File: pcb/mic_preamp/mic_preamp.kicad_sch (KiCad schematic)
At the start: 17 parts, among them J1 mic_in, J2 power_input, J3 line_out, U1 THAT1512

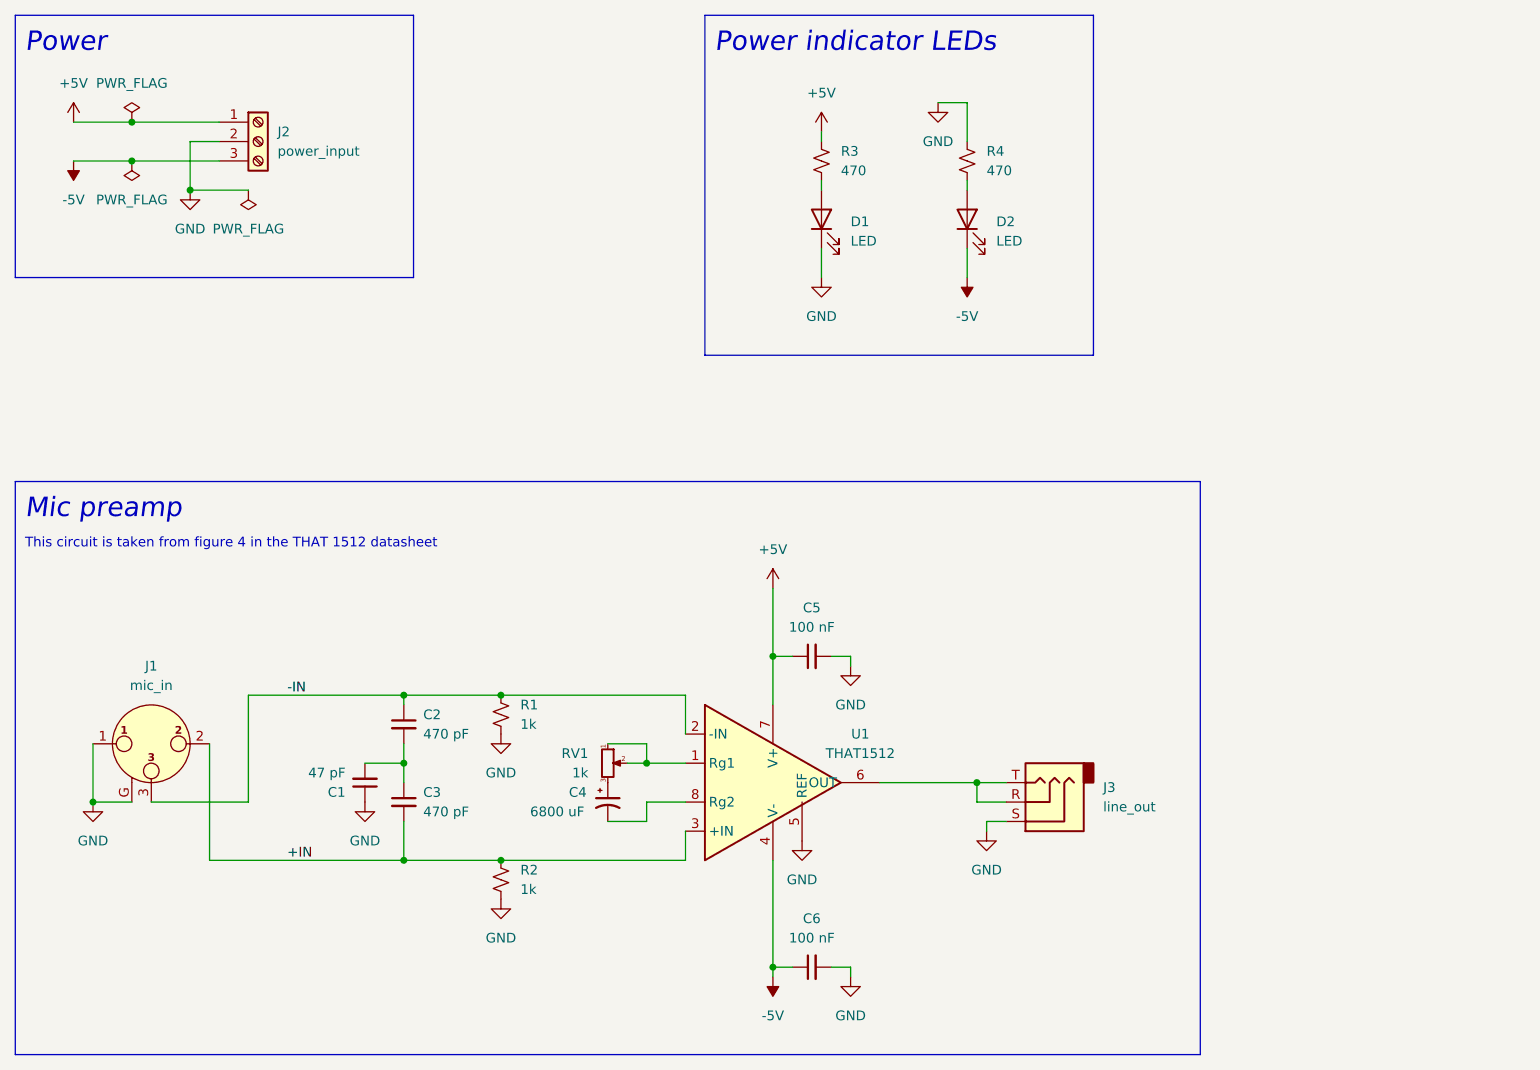
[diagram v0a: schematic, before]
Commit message: mic preamp pcb layout
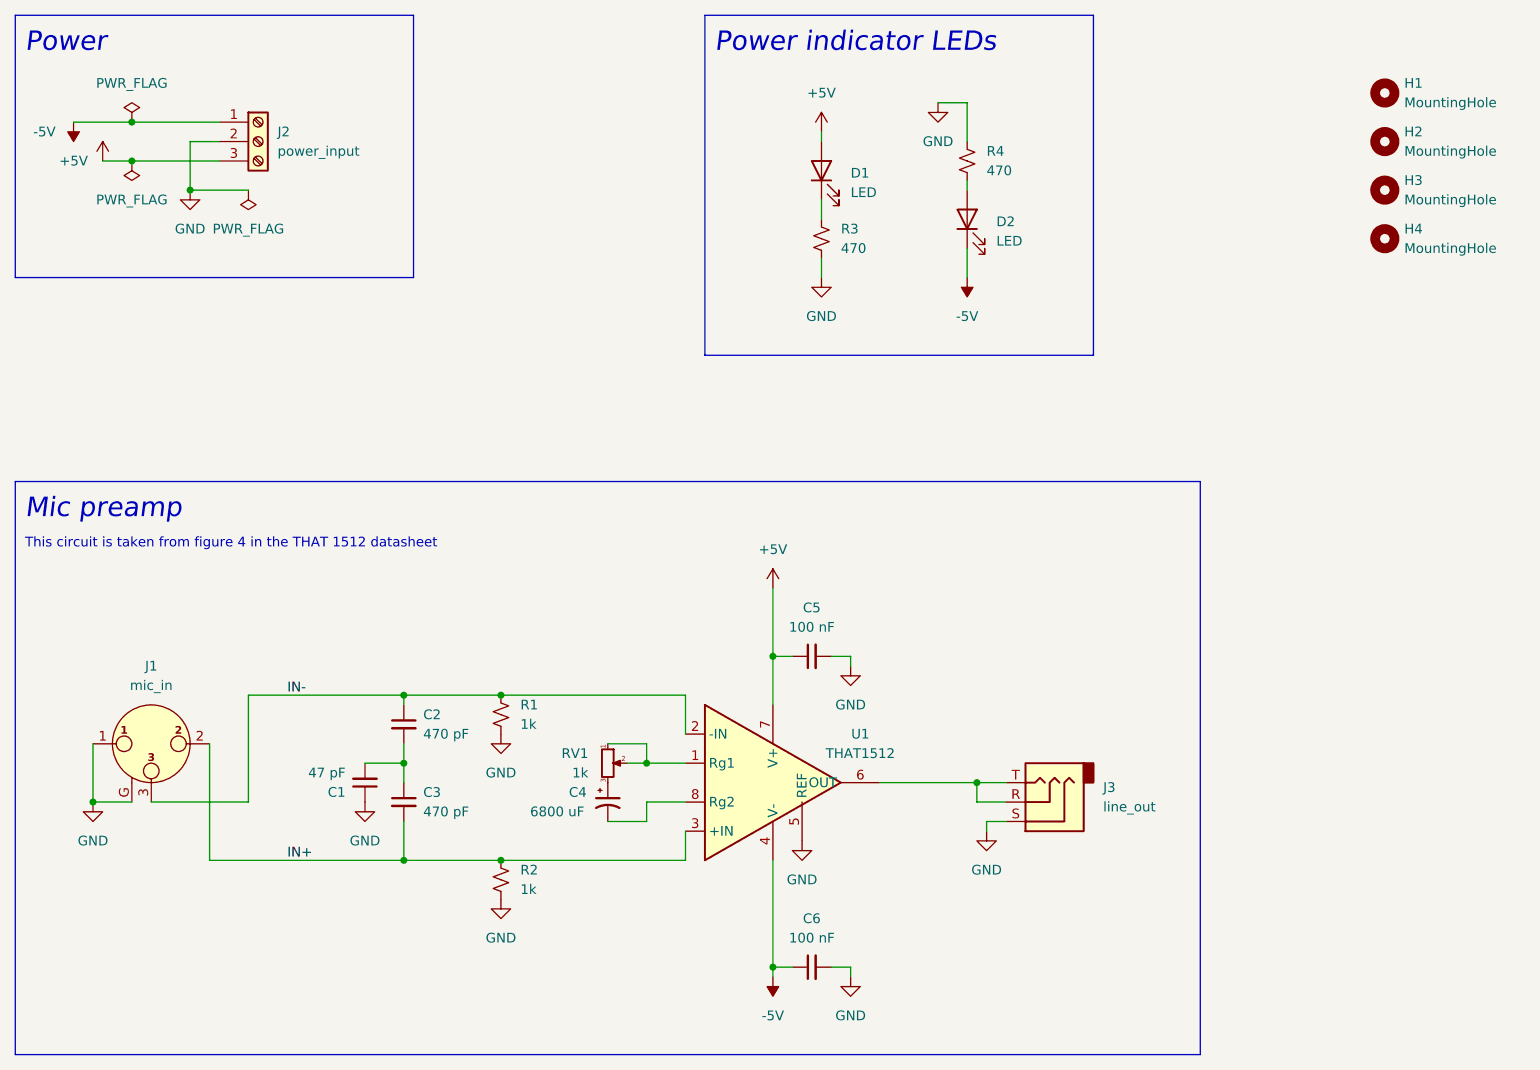
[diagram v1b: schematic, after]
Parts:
- added H1, H2, H3, H4: MountingHole, symbol Mechanical:MountingHole
- J2: footprint Capacitor_THT:C_Disc_D5.0mm_W2.5mm_P5.00mm -> TerminalBlock_Phoenix:TerminalBlock_Phoenix_MKDS-1,5-3-5.08_1x03_P5.08mm_Horizontal
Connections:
- net +5V: now also D1.2 (A), J2.3 (Pin_3); no longer J2.1 (Pin_1), R3.1
- net -5V: now also J2.1 (Pin_1); no longer J2.3 (Pin_3)
- net GND: now also R3.2; no longer D1.1 (K)
- net +IN renamed IN+
- net -IN renamed IN-
- new net: D1.1 (K), R3.1
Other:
- moved on the sheet: D1, R3

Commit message: fix mounting hole footprint
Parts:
- H1, H2, H3, H4: footprint (none) -> MountingHole:MountingHole_3.2mm_M3
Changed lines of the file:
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@@
       (effects (font (size 1.27 1.27)) (justify left))
     )
-    (property "Footprint" "" (id 2) (at 215.9 41.91 0)
+    (property "Footprint" "MountingHole:MountingHole_3.2mm_M3" (id 2) (at 215.9 41.91 0)
       (effects (font (size 1.27 1.27)) hide)
     )
@@
       (effects (font (size 1.27 1.27)) (justify left))
     )
-    (property "Footprint" "" (id 2) (at 215.9 48.26 0)
+    (property "Footprint" "MountingHole:MountingHole_3.2mm_M3" (id 2) (at 215.9 48.26 0)
       (effects (font (size 1.27 1.27)) hide)
     )
@@
       (effects (font (size 1.27 1.27)) (justify left))
     )
-    (property "Footprint" "" (id 2) (at 215.9 35.56 0)
+    (property "Footprint" "MountingHole:MountingHole_3.2mm_M3" (id 2) (at 215.9 35.56 0)
       (effects (font (size 1.27 1.27)) hide)
     )
@@
       (effects (font (size 1.27 1.27)) (justify left))
     )
-    (property "Footprint" "" (id 2) (at 215.9 29.21 0)
-      (effects (font (size 1.27 1.27)) hide)
-    )
+    (property "Footprint" "MountingHole:MountingHole_3.2mm_M3" (id 2) (at 215.9 29.21 0)
+      (effects (font (size 1.27 1.27)) hide)
+    )

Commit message: change C4 to polarized footprint
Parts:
- C4: footprint Capacitor_THT:C_Radial_D12.5mm_H25.0mm_P5.00mm -> Capacitor_THT:CP_Radial_D12.5mm_P5.00mm
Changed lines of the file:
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@@
       (effects (font (size 1.27 1.27)) (justify left))
     )
-    (property "Footprint" "Capacitor_THT:C_Radial_D12.5mm_H25.0mm_P5.00mm" (id 2) (at 114.3 121.92 0)
+    (property "Footprint" "Capacitor_THT:CP_Radial_D12.5mm_P5.00mm" (id 2) (at 114.3 121.92 0)
       (effects (font (size 1.27 1.27)) hide)
     )
@@
     )
     (path "/bd02eb54-7f11-4526-a0b5-1f059c077389"
-      (reference "C4") (unit 1) (value "6800 uF") (footprint "Capacitor_THT:C_Radial_D12.5mm_H25.0mm_P5.00mm")
+      (reference "C4") (unit 1) (value "6800 uF") (footprint "Capacitor_THT:CP_Radial_D12.5mm_P5.00mm")
     )
     (path "/50d0b2ba-285f-4c8f-a6c0-73fe2e8303b2"
